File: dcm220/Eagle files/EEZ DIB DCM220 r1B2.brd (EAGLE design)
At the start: 145 x 95 mm, 230 parts, among them IC1 Si8662AB-B-IS1, IC10 LT3763EFE#PBF, IC11 MC33274ADR2G, IC12 LT3763EFE#PBF, IC2 TPS54060DGQ, IC3 Si8641AB-B-IS1, IC4 M24C32-WMN6P, IC5 LP2985-33DBVR, IC6 TPD4E001DRLR, IC7 MAX5715BAUD+, IC8 STM32F373C8T6, IC9 MC33272ADR2G, J1 4907, J2 571-0500, J3 571-0100, J4 571-0500, J5 571-0100, Q1 IRFR7546TRPBF, Q2 IRFR7546TRPBF, Q3 2N7002, Q4 BSS84, Q5 IRFR7546TRPBF, Q6 IRFR7546TRPBF, Q7 2N7002, Q8 BSS84, X1 172648-0102, X2 77317-104-28LF, X3 22-23-2061, X4 ZL263-10DG, Y1 LF XTAL026392

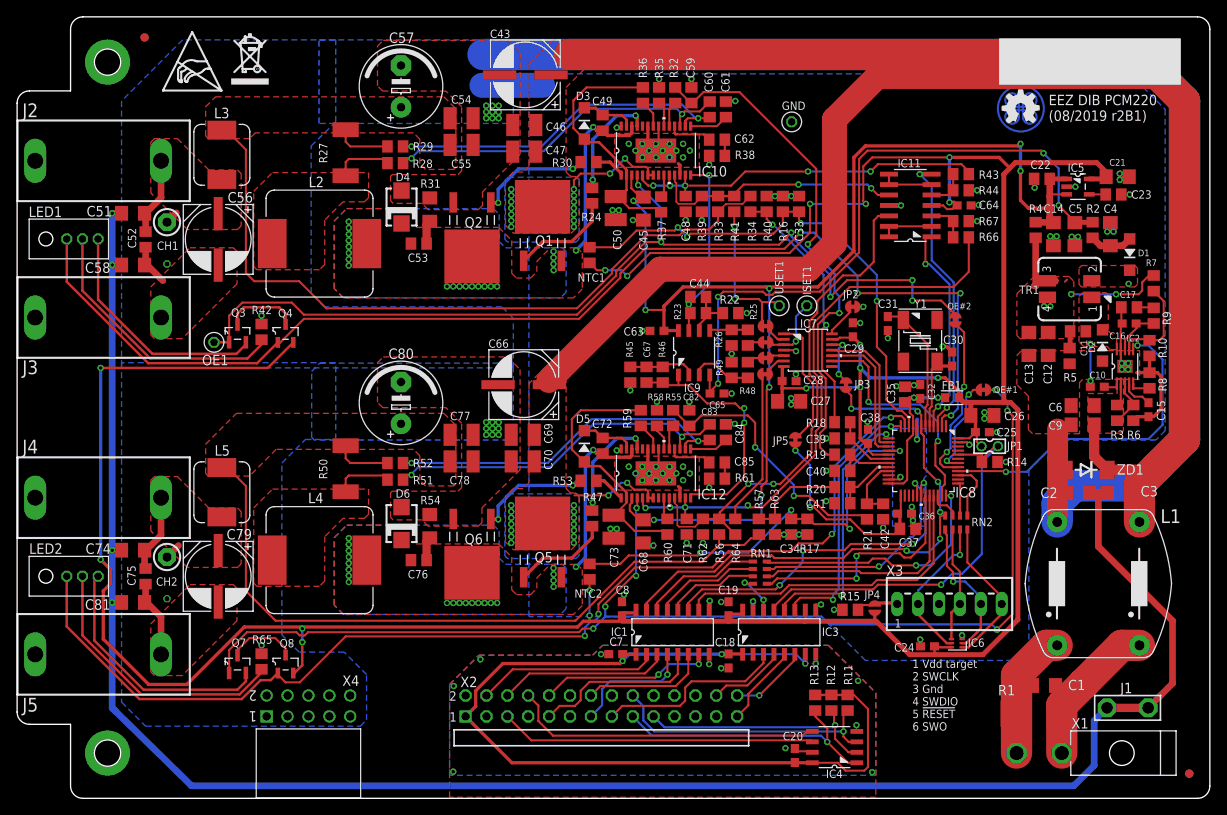
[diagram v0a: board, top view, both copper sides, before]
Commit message: DCM220, C36 value update
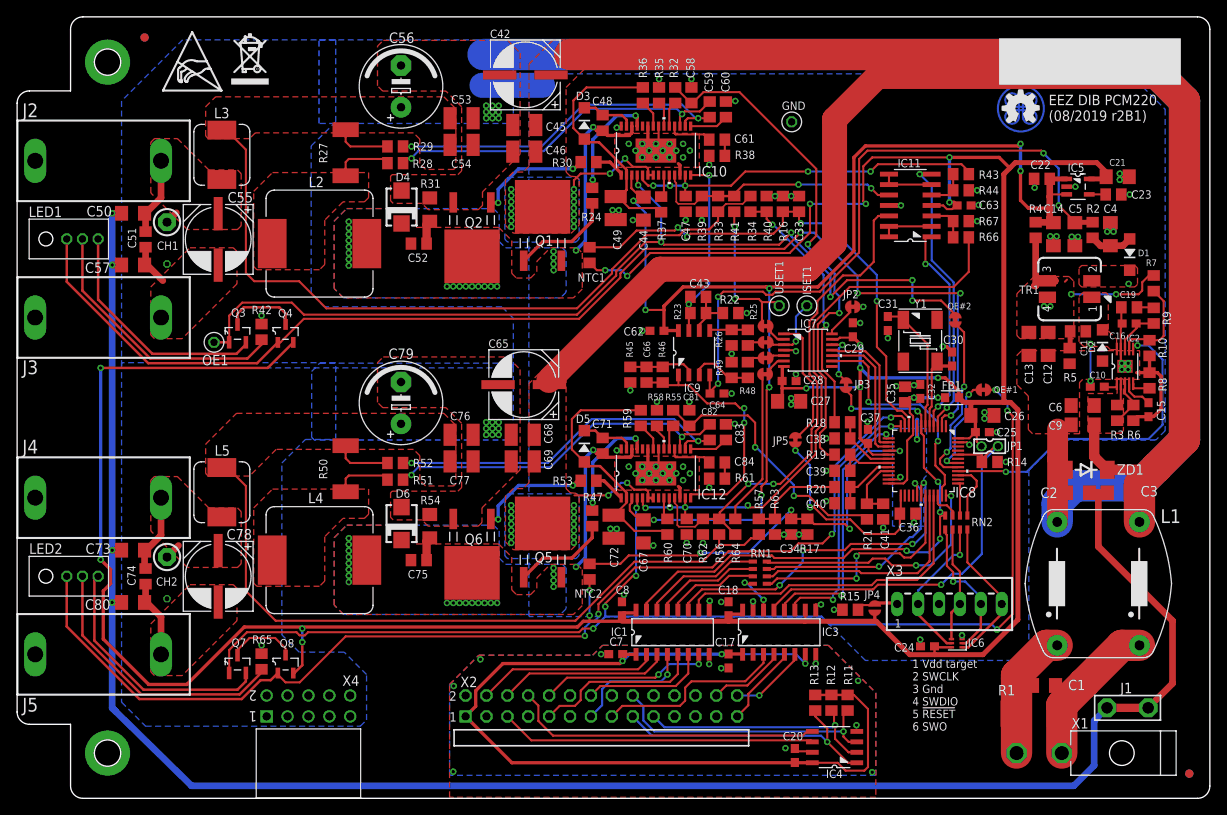
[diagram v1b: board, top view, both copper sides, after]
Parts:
- removed C85: 4n7, rcl:C0805
- C17: value 10n -> 100n; device rcl:C0805 -> rcl:C0603
- C19: value 100n -> 10n; device rcl:C0603 -> rcl:C0805
- C36: value 100n -> 100p; device rcl:C0603 -> rcl:C0805
- C37: value N.C. -> 100n; device rcl:C0805 -> rcl:C0603
- C38: value 100n -> 3n3; device rcl:C0603 -> rcl:C0805
- C42: value 3n3 -> EEEFK1V470P; device rcl:C0805 -> EEZ_Lib1:CAPAE830X1050N
- C43, C66: value EEEFK1V470P -> 100p; device EEZ_Lib1:CAPAE830X1050N -> rcl:C0805
- C44, C67: value 100p -> 4u7; device rcl:C0805 -> rcl:C1206
- C45, C68: value 4u7 -> 10u; device rcl:C1206 -> rcl:C1210
- C47, C70: value 10u -> 1u; device rcl:C1210 -> rcl:C0805
- C48, C71: value 1u -> 220n
- C49, C72: value 220n -> 22u; device rcl:C0805 -> rcl:C1210
- C50, C73: value 22u -> 10n/200V; device rcl:C1210 -> rcl:C1206
- C51, C74: value 10n/200V -> 1u; device rcl:C1206 -> rcl:C0805
- C52, C75: value 1u -> N.C.
- C53, C76: value N.C. -> 22u; device rcl:C0805 -> rcl:C1210
- C55, C78: value 22u -> EEEFK1V470P; device rcl:C1210 -> EEZ_Lib1:CAPAE830X1050N
- C56, C79: value EEEFK1V470P -> UVZ1E102MPD; device EEZ_Lib1:CAPAE830X1050N -> EEZ_Lib1:ECAP5/10.5
- C57, C80: value UVZ1E102MPD -> 10n/200V; device EEZ_Lib1:ECAP5/10.5 -> rcl:C1206
- C58, C81: value 10n/200V -> 470p; device rcl:C1206 -> rcl:C0805
- C59, C82: value 470p -> 33n
- C60, C83: value 33n -> 10n
- C61, C84: value 10n -> 4n7
- C62: value 4n7 -> 100n; device rcl:C0805 -> rcl:C0603
- C65: value 100n -> EEEFK1V470P; device rcl:C0603 -> EEZ_Lib1:CAPAE830X1050N
- moved C81 71.2 mm to (81.7, 46.2), turned to 270 degrees
- moved C58 70.9 mm to (82.0, 85.5), turned to 270 degrees
- moved C42 68.6 mm to (61.8, 87.9), turned to 180 degrees
- moved C17 65.0 mm to (86.5, 16.7), turned to 270 degrees
- moved C19 60.9 mm to (135.2, 59.7), turned to 0 degrees
- moved C50 58.7 mm to (14.1, 71.1), turned to 0 degrees
- moved C73 58.5 mm to (14.1, 30.2), turned to 0 degrees
- moved C80 40.6 mm to (14.1, 23.8), turned to 0 degrees
- moved C63 40.3 mm to (115.1, 72.1), turned to 0 degrees
- moved C57 39.2 mm to (14.1, 64.8), turned to 0 degrees
- moved C64 37.7 mm to (85.1, 49.2), turned to 180 degrees
- moved C43 34.2 mm to (82.8, 61.0), turned to 0 degrees
- moved C75 33.3 mm to (48.8, 29.0), turned to 0 degrees
- moved C52 33.2 mm to (48.8, 67.4), turned to 0 degrees
- moved C78 32.7 mm to (24.4, 27.0), turned to 270 degrees
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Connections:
- net +3V3: now also C18.2, C37.2, C63.1; no longer C19.2, C38.2, C64.1
- net +8V: now also C44.1, C62.1, C67.1; no longer C45.1, C63.1, C68.1
- net -8V: now also C64.2; no longer C65.2
- net AGND: no longer C37.1
- net DC_OUT+: now also C42.+, C45.1, C65.+, C68.1; no longer C43.+, C47.1, C66.+, C70.1
- net DC_OUT-: now also C42.-, C45.2, C51.2, C53.2, C55.-, C57.2, C65.-, C68.2, C74.2, C76.2, C78.-, C80.2; no longer C43.-, C47.2, C52.2, C55.2, C57.-, C58.2, C66.-, C70.2, C75.2, C78.2, C80.-, C81.2
- net GND: now also C18.1, C37.1, C44.2, C47.2, C49.2, C58.1, C60.1, C62.2, C64.1, C67.2, C70.2, C72.2, C81.1, C83.1; no longer C17.1, C42.1, C45.2, C48.2, C50.2, C59.1, C61.1, C64.2, C65.1, C68.2, C71.2, C73.2, C82.1, C84.1
- net GNDIO: now also C17.2; no longer C18.2
- net INTVCC1: now also C49.1; no longer C50.1
- net INTVCC2: now also C72.1; no longer C73.1
- net I_MON#1: now also C39.2; no longer C40.2
- net I_MON#2: now also C41.2; no longer C42.2
- net I_MON1: now also C58.2; no longer C59.2
- net I_MON2: now also C81.2; no longer C82.2
- net N$12: now also C60.2; no longer C61.2
- net N$13: now also C61.1; no longer C62.1
- net N$14: now also C61.2; no longer C62.2
- net N$17: now also C52.2; no longer C53.2
- net N$22: now also C48.1; no longer C49.1
- net N$249: now also C84.2; no longer C85.2
- net N$251: now also C43.2; no longer C44.2
- net N$252: now also C43.1; no longer C44.1
- net N$263: now also C75.2; no longer C76.2
- net N$264: now also C71.1; no longer C72.1
- net N$276: now also C19.2; no longer C17.2
- net N$277: now also C66.1; no longer C67.1
- net N$278: now also C66.2; no longer C67.2
- net N$36: now also C83.2; no longer C84.2
- net N$37: now also C84.1; no longer C85.1
- net N$52: no longer C37.2
- net PE: now also C50.1, C57.1, C73.1, C80.1; no longer C51.1, C58.1, C74.1, C81.1
- net SENSE1+: now also C59.1; no longer C60.1
- net SENSE1+1: now also C82.1; no longer C83.1
- net SENSE1-: now also C59.2; no longer C60.2
- net SENSE1-1: now also C82.2; no longer C83.2
- net SW1: now also C48.2, C52.1; no longer C49.2, C53.1
- net SW2: now also C71.2, C75.1; no longer C72.2, C76.1
- net U_MON#1: now also C38.2; no longer C39.2
- net U_MON#2: now also C40.2; no longer C41.2
- net V+: now also C17.1; no longer C18.1
- net VOUT1+: now also C53.1, C56.+; no longer C55.1, C57.+
- net VOUT2+: now also C76.1, C79.+; no longer C78.1, C80.+
- net VOUT_LC1+: now also C50.2, C51.1, C55.+; no longer C51.2, C52.1, C56.+
- net VOUT_LC2+: now also C73.2, C74.1, C78.+; no longer C74.2, C75.1, C79.+
- net VREF1: now also C47.1; no longer C48.1
- net VREF2: now also C70.1; no longer C71.1
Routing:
- net AGND: track 7.85 -> 6.12 mm, vias 4 -> 3

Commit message: DCM220 R8 value fixed
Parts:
- R8: value 330R -> 330K
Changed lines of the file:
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@@
 <attribute name="VALUE" x="137.922" y="45.466" size="1.016" layer="27" ratio="10" rot="R90"/>
 </element>
-<element name="R8" library="rcl" package="R0805" value="330R" x="137.668" y="50.8" smashed="yes" rot="R270">
+<element name="R8" library="rcl" package="R0805" value="330K" x="137.668" y="50.8" smashed="yes" rot="R270">
 <attribute name="NAME" x="139.7635" y="49.4665" size="1.016" layer="25" ratio="10" rot="R90"/>
 <attribute name="VALUE" x="138.1125" y="48.9585" size="1.016" layer="27" ratio="10" rot="R90"/>

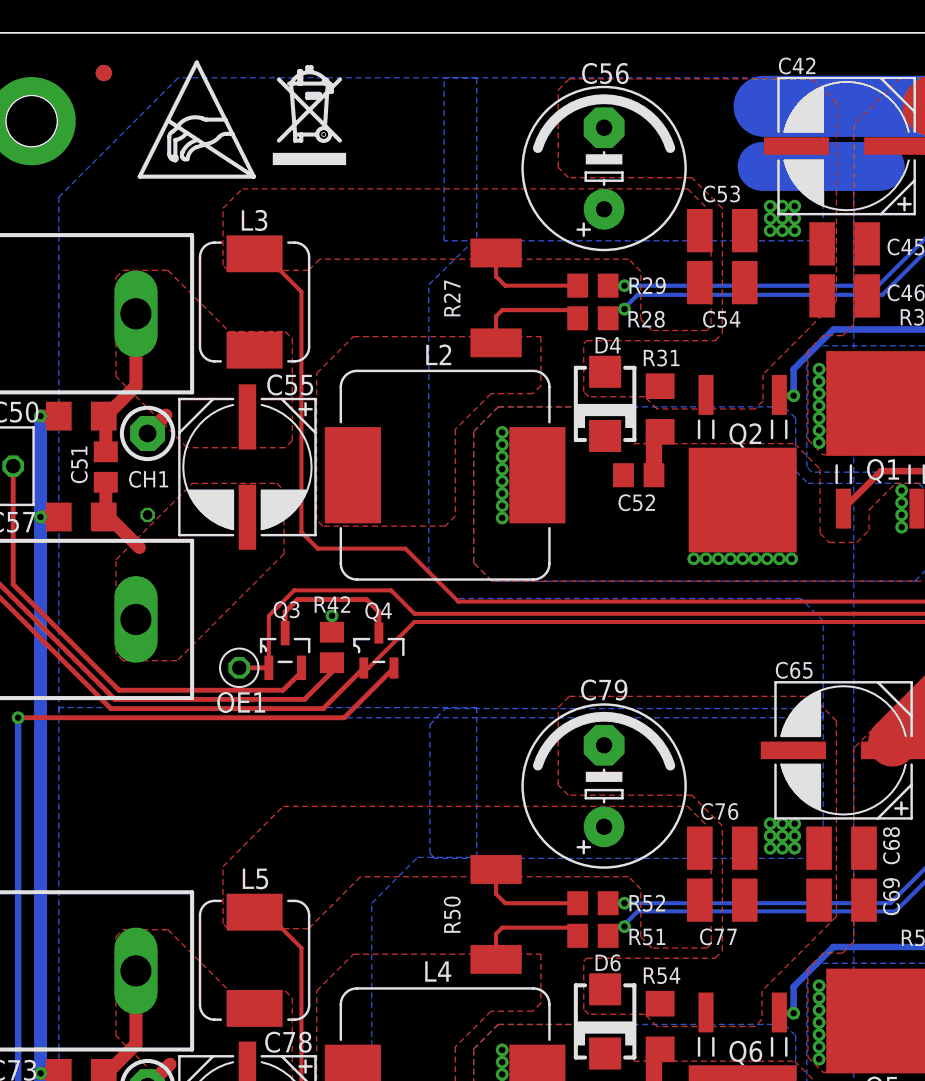
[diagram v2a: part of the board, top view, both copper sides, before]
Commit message: TVS added on outputs
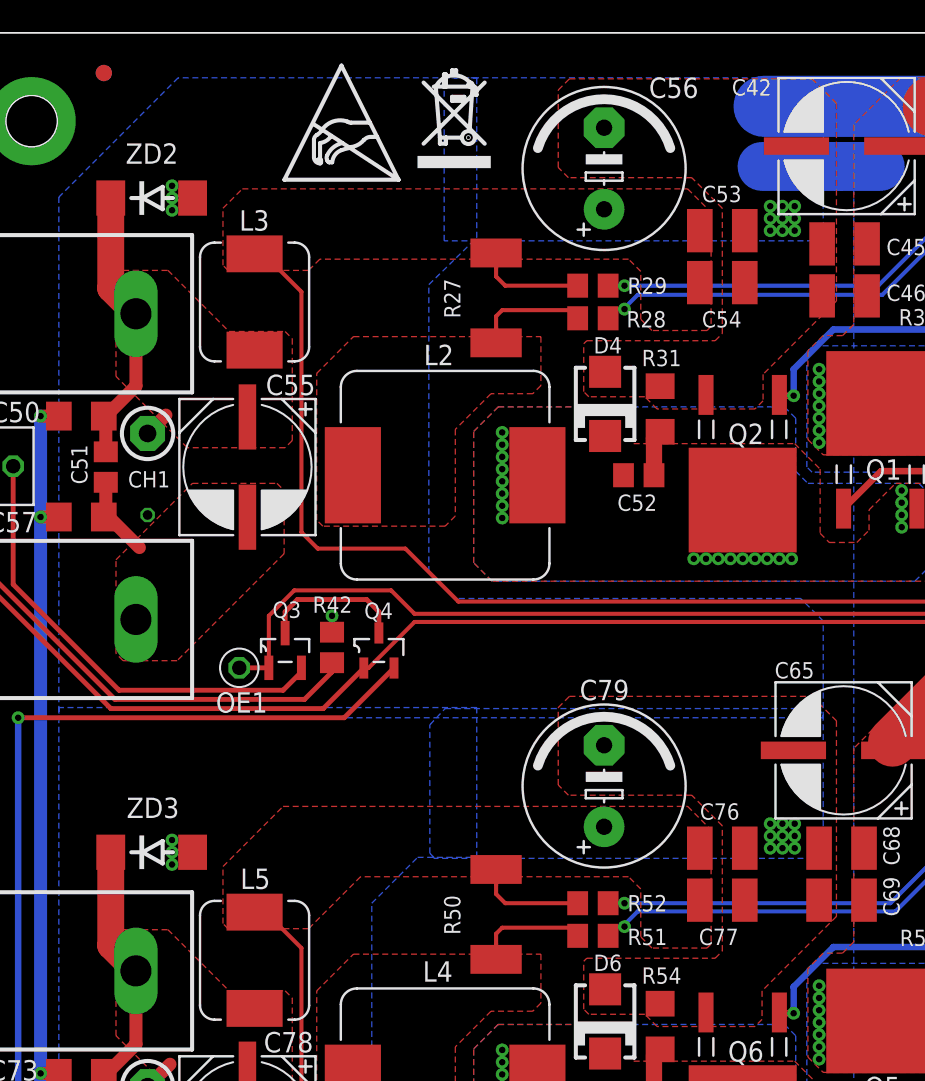
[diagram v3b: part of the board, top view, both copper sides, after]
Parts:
- added ZD2, ZD3: SMAJ51A, EEZ_Lib1:DO214AA
- moved U$2 9.02 mm to (35.0, 86.6)
- moved U$4 9.02 mm to (26.8, 85.9)
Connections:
- net DC_OUT-: now also ZD2.A, ZD3.A
- net VOUT_LC1+: now also ZD2.C
- net VOUT_LC2+: now also ZD3.C
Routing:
- net VOUT_LC2+: track 11.6 -> 19.6 mm
- net VOUT_LC1+: track 11.2 -> 19.0 mm
- net DC_OUT-: track 185.5 -> 188.1 mm, vias 20 -> 26
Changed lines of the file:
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@@
 <attribute name="VALUE" x="95.8056" y="5.888" size="0.8128" layer="27" ratio="10" rot="SR0"/>
 </element>
-<element name="U$4" library="olimex_logo1" package="ESD_SYMBOL" value="" x="17.734" y="86.042" smashed="yes"/>
-<element name="U$2" library="olimex_logo1" package="RECYCLE_BIN1/8" value="" x="26.0245" y="86.7625" smashed="yes"/>
+<element name="U$4" library="olimex_logo1" package="ESD_SYMBOL" value="" x="26.751" y="85.8515" smashed="yes"/>
+<element name="U$2" library="olimex_logo1" package="RECYCLE_BIN1/8" value="" x="35.0415" y="86.572" smashed="yes"/>
 <element name="C7" library="rcl" package="C0603" value="100n" x="72.771" y="17.526" smashed="yes" rot="R180">
 <attribute name="NAME" x="72.009" y="18.542" size="1.016" layer="25" ratio="10"/>
@@
 </element>
 <element name="C42" library="EEZ_Lib1" package="CAPAE830X1050N" value="EEEFK1V470P" x="61.7855" y="87.9475" smashed="yes" rot="R180">
-<attribute name="NAME" x="57.4929" y="92.4306" size="1.016" layer="25" ratio="10" rot="SR0"/>
+<attribute name="NAME" x="54.6354" y="91.0971" size="1.016" layer="25" ratio="10" rot="SR0"/>
 <attribute name="VALUE" x="56.8325" y="87.4903" size="1.016" layer="27" ratio="10" rot="SR0"/>
 </element>
@@
 </element>
 <element name="C56" library="EEZ_Lib1" package="ECAP5/10.5" value="UVZ1E102MPD" x="46.6725" y="86.5505" smashed="yes" rot="R90">
-<attribute name="NAME" x="45.212" y="91.8337" size="1.27" layer="25" ratio="10"/>
+<attribute name="NAME" x="49.4665" y="90.9447" size="1.27" layer="25" ratio="10"/>
 <attribute name="VALUE" x="41.7703" y="85.9917" size="1.016" layer="27" ratio="10"/>
 </element>
@@
 <attribute name="VALUE" x="14.986" y="28.0035" size="1.27" layer="27" rot="R270"/>
 </element>
+<element name="ZD2" library="EEZ_Lib1" package="DO214AA" value="SMAJ51A" x="18.4785" y="84.709" smashed="yes">
+<attribute name="NAME" x="16.8545" y="86.8435" size="1.27" layer="25" ratio="10"/>
+<attribute name="VALUE" x="14.6955" y="84.0985" size="1.27" layer="27" ratio="10"/>
+</element>
+<element name="ZD3" library="EEZ_Lib1" package="DO214AA" value="SMAJ51A" x="18.4785" y="43.942" smashed="yes">
+<attribute name="NAME" x="16.918" y="46.0765" size="1.27" layer="25" ratio="10"/>
+<attribute name="VALUE" x="14.505" y="43.3315" size="1.27" layer="27" ratio="10"/>
+</element>
 </elements>
 <signals>
@@
 <wire x1="15.497" y1="23.8125" x2="15.751" y2="23.8125" width="0.8128" layer="1"/>
 <wire x1="15.751" y1="23.8125" x2="17.5" y2="22.0635" width="0.8128" layer="1"/>
+<contactref element="ZD2" pad="A"/>
+<contactref element="ZD3" pad="A"/>
+<via x="19.7485" y="43.942" extent="1-16" drill="0.4" shape="square"/>
+<via x="19.7485" y="44.704" extent="1-16" drill="0.4" shape="square"/>
+<via x="19.7485" y="43.18" extent="1-16" drill="0.4" shape="square"/>
+<wire x1="19.7485" y1="43.942" x2="21.0285" y2="43.942" width="0.4064" layer="1"/>
+<via x="19.7485" y="84.709" extent="1-16" drill="0.4" shape="square"/>
+<via x="19.7485" y="85.471" extent="1-16" drill="0.4" shape="square"/>
+<via x="19.7485" y="83.947" extent="1-16" drill="0.4" shape="square"/>
+<wire x1="21.0285" y1="84.709" x2="19.7485" y2="84.709" width="0.4064" layer="1"/>
 <wire x1="61.16" y1="86.6775" x2="61.2235" y2="85.471" width="0" layer="19" extent="16-16"/>
 <wire x1="2.2" y1="17.5" x2="15.497" y2="23.8125" width="0" layer="19" extent="1-1"/>
@@
 <wire x1="15.497" y1="71.12" x2="15.624" y2="71.12" width="0.8128" layer="1"/>
 <wire x1="15.624" y1="71.12" x2="17.5" y2="72.996" width="0.8128" layer="1"/>
-<wire x1="15.497" y1="71.12" x2="2.2" y2="77.5" width="0" layer="19" extent="1-1"/>
+<contactref element="ZD2" pad="C"/>
+<wire x1="15.9285" y1="84.709" x2="15.9285" y2="79.0715" width="1.6764" layer="1"/>
+<wire x1="15.9285" y1="79.0715" x2="17.5" y2="77.5" width="1.6764" layer="1"/>
+<wire x1="15.9285" y1="79.0715" x2="2.2" y2="77.5" width="0" layer="19" extent="1-1"/>
 </signal>
 <signal name="VOUT_LC2+">
@@
 <wire x1="15.497" y1="30.1625" x2="15.497" y2="28.0615" width="0.8128" layer="1"/>
 <wire x1="15.497" y1="28.0615" x2="15.621" y2="27.9375" width="0.8128" layer="1"/>
-<wire x1="15.497" y1="30.1625" x2="2.2" y2="36.55" width="0" layer="19" extent="1-1"/>
+<contactref element="ZD3" pad="C"/>
+<wire x1="15.9285" y1="43.942" x2="15.9285" y2="38.1215" width="1.6764" layer="1"/>
+<wire x1="15.9285" y1="38.1215" x2="17.5" y2="36.55" width="1.6764" layer="1"/>
+<wire x1="15.9285" y1="38.1215" x2="2.2" y2="36.55" width="0" layer="19" extent="1-1"/>
 </signal>
 <signal name="N$270">

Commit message: update TME connectors in BOMs
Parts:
- X4: value ZL263-10DG -> DS1024-2*5R0
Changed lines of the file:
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@@
 <attribute name="VALUE" x="106.2355" y="56.642" size="0.8128" layer="27" ratio="10" rot="R90"/>
 </element>
-<element name="X4" library="EEZ_connectors" package="SSW-105-02-T-D-RA" value="ZL263-10DG" x="40.5" y="12.5" locked="yes" smashed="yes" rot="R180">
+<element name="X4" library="EEZ_connectors" package="SSW-105-02-T-D-RA" value="DS1024-2*5R0" x="40.5" y="12.5" locked="yes" smashed="yes" rot="R180">
 <attribute name="FARNELL" value="2308470" x="40.5" y="12.5" size="1.016" layer="27" ratio="10" rot="R180" display="off"/>
 <attribute name="NAME" x="39.5354" y="13.6747" size="1.27" layer="25" ratio="10" rot="SR0"/>
